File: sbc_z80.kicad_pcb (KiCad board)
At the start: 4 copper layers, 102.6 x 50.8 mm, 95 parts, among them J1 RC80 Bus, J2 CTC Header, J3 AVR-JTAG-10, J4 IDE, J5 PIO Header, J6 Port A, J7 Port B, J8 USB_B_Micro, Q1 IRLML6402, SW1 Reset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

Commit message: more routing
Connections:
- J1 pad 21: /CLK -> /CLK_CPU
- U3 pad 1: /CLK -> /CLK_CPU
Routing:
- net /D1: track 1.23 -> 186.7 mm, vias 1 -> 15
- net /D5: track 0.00 -> 179.5 mm, vias 0 -> 12
- net /D4: track 1.40 -> 170.8 mm, vias 0 -> 12
- net /D6: track 2.35 -> 168.4 mm, vias 1 -> 11
- net /IEI: track 0.00 -> 132.6 mm, vias 0 -> 6
- net /D7: track 0.00 -> 123.6 mm, vias 0 -> 6
- net /D3: track 0.00 -> 121.5 mm, vias 0 -> 12
- net /~M1: track 0.00 -> 114.5 mm, vias 0 -> 7
- net /D0: track 19.2 -> 121.3 mm, vias 0 -> 10
- net /~RESET: track 0.00 -> 101.2 mm, vias 0 -> 5
- net /D2: track 9.98 -> 110.8 mm, vias 2 -> 9
- net /CLK_CPU: track 0.00 -> 91.1 mm, vias 0 -> 6
- net /~IORQ: track 0.00 -> 75.4 mm, vias 0 -> 3
- net /~INT: track 0.00 -> 60.1 mm, vias 0 -> 3
- net /~WR: track 0.00 -> 58.1 mm, vias 0 -> 3
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
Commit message: cleanup
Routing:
- net /D7: track 123.6 -> 145.9 mm, vias 6 -> 7
- net /IEI: track 132.6 -> 134.1 mm
- net /D6: track 168.4 -> 167.6 mm
- net /PA4: track 27.4 -> 26.9 mm
- net /D3: track 121.5 -> 121.7 mm, vias 12 -> 11
- net /D1: vias 15 -> 14

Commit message: checkpoint
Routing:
- net /~IORQ: track 75.4 -> 0.00 mm, vias 3 -> 0
- net /~RTSB: track 0.00 -> 18.4 mm, vias 0 -> 3
- net /D2: track 110.4 -> 125.5 mm
- net /TXB: track 13.2 -> 27.8 mm, vias 0 -> 1
- net /~M1: track 114.5 -> 106.7 mm, vias 7 -> 6
- net /D7: track 145.9 -> 141.0 mm
- net /PA1: track 18.7 -> 20.5 mm
- net Net-(J7-Pad6): track 4.26 -> 5.92 mm, vias 0 -> 1
- net Net-(J7-Pad5): track 2.94 -> 4.38 mm, vias 0 -> 1
- net /PB2: track 9.20 -> 10.1 mm, vias 0 -> 1
- net /PB3: track 9.92 -> 10.8 mm, vias 0 -> 1
- net /TDI: track 4.12 -> 3.32 mm
- net /~ASTB: track 19.3 -> 18.5 mm
- net /D4: track 170.8 -> 171.6 mm
- net /A0: track 167.6 -> 166.9 mm
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- added copper zone on In2.Cu, net (none)
- removed copper zone on In2.Cu, net VCC

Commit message: routed...
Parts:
- C1, C10, C15, C16, C2, C5, C6, C8, C9, R10, R12, R13, R14, R15: moved to F.Cu
- moved R11 12.7 mm to (154.3, 105.2), turned to 0 degrees
- moved C16 5.97 mm to (164.5, 94.9), turned to 0 degrees
- moved C8 4.99 mm to (190.4, 91.6)
- moved C1 4.91 mm to (127.0, 115.7), turned to 270 degrees
- moved C5 4.84 mm to (127.0, 101.7), turned to 90 degrees
- moved C15 4.36 mm to (190.0, 107.2)
- moved C2 4.35 mm to (116.5, 107.3)
- moved C6 3.72 mm to (133.9, 92.3)
- moved C10 3.35 mm to (176.7, 99.7)
- moved C9 1.39 mm to (150.7, 98.8)
- moved Q1 1.02 mm to (116.3, 106.6)
- moved R35 0.64 mm to (196.6, 113.4)
- moved R9 0.64 mm to (109.1, 121.0)
- moved R6 0.63 mm to (109.1, 116.0)
- moved R7 0.63 mm to (109.1, 110.9)
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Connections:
- C13 pad 1: +5V -> VCC
- C14 pad 1: +5V -> VCC
- J1 pad 37: (no net) -> /USR1
- J1 pad 38: (no net) -> /USR2
- J1 pad 39: (no net) -> /USR3
- J1 pad 41: (no net) -> Net-(J1-Pad41)
- J1 pad 42: (no net) -> Net-(J1-Pad42)
- J1 pad 43: (no net) -> Net-(J1-Pad43)
- J1 pad 44: (no net) -> Net-(J1-Pad44)
- J1 pad 45: (no net) -> Net-(J1-Pad45)
- J1 pad 46: (no net) -> Net-(J1-Pad46)
- J1 pad 47: (no net) -> Net-(J1-Pad47)
- J1 pad 48: (no net) -> Net-(J1-Pad48)
- J1 pad 49: (no net) -> /A23
- J1 pad 50: (no net) -> /A22
- J1 pad 51: (no net) -> /A21
- J1 pad 52: (no net) -> /A20
- J1 pad 53: (no net) -> /A19
- J1 pad 61: (no net) -> /CLK2
- J1 pad 67: (no net) -> /D8
- J1 pad 68: (no net) -> /D9
- J1 pad 69: (no net) -> /D10
- J1 pad 70: (no net) -> /D11
- J1 pad 71: (no net) -> /D12
- J1 pad 72: (no net) -> /D13
- J1 pad 73: (no net) -> /D14
- J1 pad 74: (no net) -> /D15
- J1 pad 77: (no net) -> /USR5
- J1 pad 78: (no net) -> /USR6
- J1 pad 79: (no net) -> /USR7
- J2 pad 9: (no net) -> /CLKX
- J3 pad 7: (no net) -> Net-(J3-Pad7)
- J3 pad 8: (no net) -> Net-(J3-Pad8)
- J4 pad 10: (no net) -> Net-(J4-Pad10)
- J4 pad 12: (no net) -> Net-(J4-Pad12)
- J4 pad 14: (no net) -> Net-(J4-Pad14)
- J4 pad 16: (no net) -> Net-(J4-Pad16)
- J4 pad 18: (no net) -> Net-(J4-Pad18)
- J4 pad 21: (no net) -> Net-(J4-Pad21)
- J4 pad 27: (no net) -> Net-(J4-Pad27)
- J4 pad 28: (no net) -> Net-(J4-Pad28)
- J4 pad 31: (no net) -> Net-(J4-Pad31)
- J4 pad 32: (no net) -> Net-(J4-Pad32)
- J4 pad 4: (no net) -> Net-(J4-Pad4)
- J4 pad 6: (no net) -> Net-(J4-Pad6)
- J4 pad 8: (no net) -> Net-(J4-Pad8)
- J6 pad 3: (no net) -> Net-(J6-Pad3)
- J7 pad 3: (no net) -> Net-(J7-Pad3)
- J8 pad 2: (no net) -> Net-(J8-Pad2)
- J8 pad 3: (no net) -> Net-(J8-Pad3)
- J8 pad 4: (no net) -> Net-(J8-Pad4)
- U10 pad 2: (no net) -> Net-(U10-Pad2)
- U10 pad 28: (no net) -> Net-(U10-Pad28)
- U10 pad 39: (no net) -> Net-(U10-Pad39)
- U12 pad 4: (no net) -> Net-(U12-Pad4)
- U12 pad 5: +5V -> VCC
- U3 pad 11: (no net) -> Net-(U3-Pad11)
- U3 pad 17: (no net) -> Net-(U3-Pad17)
- U3 pad 33: (no net) -> Net-(U3-Pad33)
- U3 pad 39: (no net) -> Net-(U3-Pad39)
- U4 pad 11: (no net) -> Net-(U4-Pad11)
- U4 pad 15: (no net) -> Net-(U4-Pad15)
- U4 pad 17: (no net) -> Net-(U4-Pad17)
- U4 pad 20: (no net) -> Net-(U4-Pad20)
- U4 pad 24: (no net) -> Net-(U4-Pad24)
- U4 pad 26: (no net) -> Net-(U4-Pad26)
- U4 pad 28: (no net) -> Net-(U4-Pad28)
- U4 pad 30: (no net) -> Net-(U4-Pad30)
- U4 pad 31: /~SIO -> /~CTC
- U4 pad 34: (no net) -> Net-(U4-Pad34)
- U4 pad 38: (no net) -> Net-(U4-Pad38)
- U4 pad 39: (no net) -> Net-(U4-Pad39)
- U4 pad 42: (no net) -> Net-(U4-Pad42)
- U4 pad 44: (no net) -> Net-(U4-Pad44)
- U4 pad 5: (no net) -> Net-(U4-Pad5)
- U4 pad 6: (no net) -> Net-(U4-Pad6)
- U4 pad 7: (no net) -> Net-(U4-Pad7)
- U5 pad 20: (no net) -> Net-(U5-Pad20)
- U5 pad 21: (no net) -> Net-(U5-Pad21)
- U5 pad 22: (no net) -> /~PIO_RST
- U5 pad 31: (no net) -> /~CTC
- U9 pad 1: (no net) -> Net-(U9-Pad1)
- U9 pad 10: (no net) -> Net-(U9-Pad10)
- U9 pad 15: (no net) -> Net-(U9-Pad15)
- U9 pad 16: (no net) -> Net-(U9-Pad16)
- U9 pad 17: (no net) -> Net-(U9-Pad17)
- U9 pad 27: (no net) -> /DO
- U9 pad 28: (no net) -> Net-(U9-Pad28)
- U9 pad 38: (no net) -> Net-(U9-Pad38)
- U9 pad 39: (no net) -> Net-(U9-Pad39)
- U9 pad 40: (no net) -> Net-(U9-Pad40)
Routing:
- net /~IORQ: track 0.00 -> 170.4 mm, vias 0 -> 10
- net /~RD: track 21.8 -> 192.0 mm, vias 3 -> 12
- net /CLK_U: track 6.93 -> 143.0 mm, vias 0 -> 5
- net /IEO: track 0.00 -> 136.1 mm, vias 0 -> 5
- net /D2: track 125.5 -> 226.4 mm, vias 9 -> 13
- net /~RESET: track 101.2 -> 190.3 mm, vias 5 -> 13
- net VCC: track 0.00 -> 86.8 mm, vias 0 -> 35
- net /D0: track 121.1 -> 206.6 mm, vias 10 -> 14
- net /~SIO: track 0.00 -> 79.1 mm, vias 0 -> 3
- net /D3: track 122.3 -> 199.8 mm, vias 10 -> 12
- net /D7: track 141.0 -> 208.4 mm, vias 7 -> 10
- net GND: track 0.00 -> 66.7 mm, vias 0 -> 36
- net /~INT: track 60.5 -> 125.8 mm, vias 3 -> 8
- net /D4: track 171.6 -> 235.6 mm, vias 12 -> 13
- net /~RAM: track 0.00 -> 63.8 mm, vias 0 -> 2
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- added copper zone on In2.Cu, net VCC
- removed copper zone on In2.Cu, net (none)

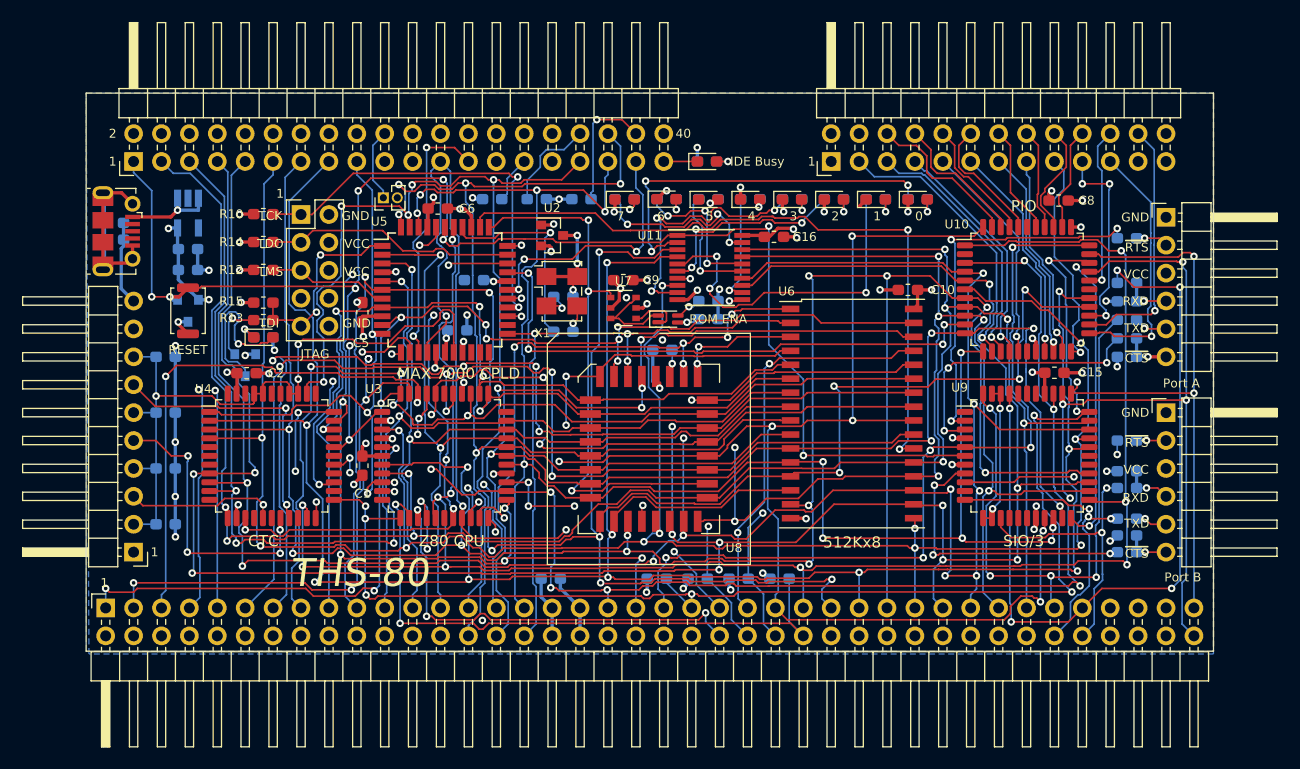
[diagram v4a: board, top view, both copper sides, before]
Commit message: passed drc
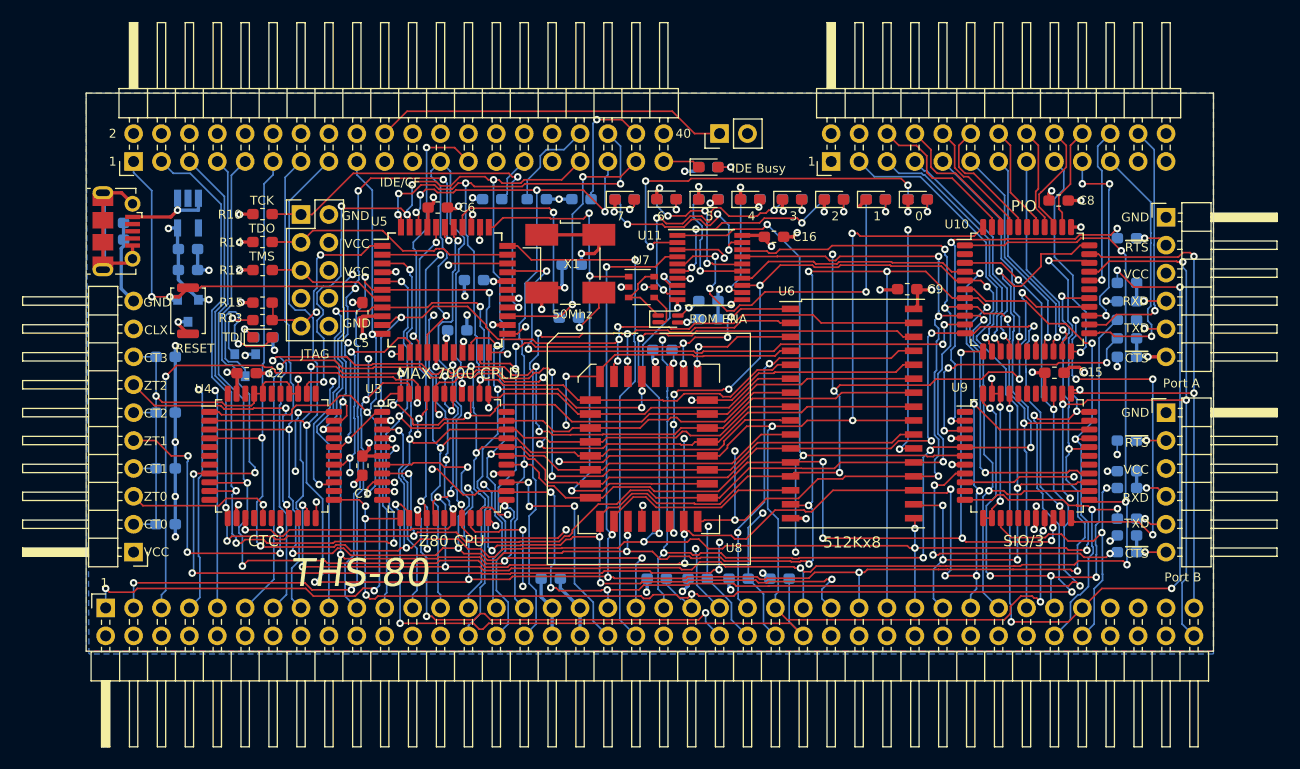
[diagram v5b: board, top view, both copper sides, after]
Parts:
- removed C10: 100nF, Capacitor_SMD:C_0603_1608Metric_Pad1.05x0.95mm_HandSolder
- removed G***: LOGO, Logos:asian_tiger
- removed U2: AP7381-33SA, Package_TO_SOT_SMD:SOT-23
- C13: value 10uF -> 1uF
- C14: value 1uF -> 100nF
- JP1: footprint Connector_PinHeader_1.27mm:PinHeader_1x02_P1.27mm_Vertical -> Connector_PinHeader_2.54mm:PinHeader_1x02_P2.54mm_Vertical
- X1: value CTX-636 50mhz -> CFPS-72 50mhz; footprint Oscillator:Oscillator_SMD_TXC_7C-4Pin_5.0x3.2mm_HandSoldering -> Oscillator:Oscillator_SMD_SeikoEpson_SG8002CA-4Pin_7.0x5.0mm_HandSoldering
- moved JP1 31.2 mm to (159.5, 85.5)
- moved C9 25.9 mm to (176.6, 99.6)
- moved C7 3.02 mm to (146.1, 97.4)
- moved X1 2.62 mm to (145.9, 97.3)
- moved U7 2.52 mm to (152.4, 99.4)
- moved R3 1.37 mm to (145.8, 102.2)
- moved D2 0.52 mm to (158.5, 88.5)
- moved R16 0.52 mm to (158.5, 88.5)
- moved C6 0.09 mm to (133.9, 92.2)
- moved D1 0.08 mm to (117.9, 104.0)
- moved R10 0.08 mm to (117.9, 92.8)
- moved R13 0.08 mm to (117.9, 102.4)
- moved R14 0.08 mm to (117.9, 95.3)
- moved R15 0.08 mm to (117.9, 100.9)
- moved R12 0.07 mm to (117.9, 97.9)
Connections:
- net /~CTC renamed /CTC_~CE~
- net /~PIO renamed /PIO_~CE~
- net /~RAM renamed /RAM_~CE~
- net /~ROM renamed /ROM_~CE~
- C7 pad 1: /3V3 -> VCC
- J1 pad 37: /USR1 -> (no net)
- J1 pad 38: /USR2 -> (no net)
- J1 pad 39: /USR3 -> (no net)
- J1 pad 41: Net-(J1-Pad41) -> (no net)
- J1 pad 42: Net-(J1-Pad42) -> (no net)
- J1 pad 43: Net-(J1-Pad43) -> (no net)
- J1 pad 44: Net-(J1-Pad44) -> (no net)
- J1 pad 45: Net-(J1-Pad45) -> (no net)
- J1 pad 46: Net-(J1-Pad46) -> (no net)
- J1 pad 47: Net-(J1-Pad47) -> (no net)
- J1 pad 48: Net-(J1-Pad48) -> (no net)
- J1 pad 49: /A23 -> (no net)
- J1 pad 50: /A22 -> (no net)
- J1 pad 51: /A21 -> (no net)
- J1 pad 52: /A20 -> (no net)
- J1 pad 53: /A19 -> (no net)
- J1 pad 61: /CLK2 -> (no net)
- J1 pad 67: /D8 -> (no net)
- J1 pad 68: /D9 -> (no net)
- J1 pad 69: /D10 -> (no net)
- J1 pad 70: /D11 -> (no net)
- J1 pad 71: /D12 -> (no net)
- J1 pad 72: /D13 -> (no net)
- J1 pad 73: /D14 -> (no net)
- J1 pad 74: /D15 -> (no net)
- J1 pad 77: /USR5 -> (no net)
- J1 pad 78: /USR6 -> (no net)
- J1 pad 79: /USR7 -> (no net)
- J2 pad 9: /CLKX -> (no net)
- J3 pad 7: Net-(J3-Pad7) -> (no net)
- J3 pad 8: Net-(J3-Pad8) -> (no net)
- J4 pad 10: Net-(J4-Pad10) -> (no net)
- J4 pad 12: Net-(J4-Pad12) -> (no net)
- J4 pad 14: Net-(J4-Pad14) -> (no net)
- J4 pad 16: Net-(J4-Pad16) -> (no net)
- J4 pad 18: Net-(J4-Pad18) -> (no net)
- J4 pad 21: Net-(J4-Pad21) -> (no net)
- J4 pad 27: Net-(J4-Pad27) -> (no net)
- J4 pad 28: Net-(J4-Pad28) -> (no net)
- J4 pad 31: Net-(J4-Pad31) -> (no net)
- J4 pad 32: Net-(J4-Pad32) -> (no net)
- J4 pad 37: /~CF -> /IDE_~CE~
- J4 pad 4: Net-(J4-Pad4) -> (no net)
- J4 pad 6: Net-(J4-Pad6) -> (no net)
- J4 pad 8: Net-(J4-Pad8) -> (no net)
- J6 pad 3: Net-(J6-Pad3) -> (no net)
- J7 pad 3: Net-(J7-Pad3) -> (no net)
- J8 pad 2: Net-(J8-Pad2) -> (no net)
- J8 pad 3: Net-(J8-Pad3) -> (no net)
- J8 pad 4: Net-(J8-Pad4) -> (no net)
- U10 pad 2: Net-(U10-Pad2) -> (no net)
- U10 pad 28: Net-(U10-Pad28) -> (no net)
- U10 pad 39: Net-(U10-Pad39) -> (no net)
- U12 pad 4: Net-(U12-Pad4) -> (no net)
- U3 pad 11: Net-(U3-Pad11) -> (no net)
- U3 pad 17: Net-(U3-Pad17) -> (no net)
- U3 pad 33: Net-(U3-Pad33) -> (no net)
- U3 pad 39: Net-(U3-Pad39) -> (no net)
- U4 pad 11: Net-(U4-Pad11) -> (no net)
- U4 pad 15: Net-(U4-Pad15) -> (no net)
- U4 pad 17: Net-(U4-Pad17) -> (no net)
- U4 pad 20: Net-(U4-Pad20) -> (no net)
- U4 pad 24: Net-(U4-Pad24) -> (no net)
- U4 pad 26: Net-(U4-Pad26) -> (no net)
- U4 pad 28: Net-(U4-Pad28) -> (no net)
- U4 pad 30: Net-(U4-Pad30) -> (no net)
- U4 pad 34: Net-(U4-Pad34) -> (no net)
- U4 pad 38: Net-(U4-Pad38) -> (no net)
- U4 pad 39: Net-(U4-Pad39) -> (no net)
- U4 pad 42: Net-(U4-Pad42) -> (no net)
- U4 pad 44: Net-(U4-Pad44) -> (no net)
- U4 pad 5: Net-(U4-Pad5) -> (no net)
- U4 pad 6: Net-(U4-Pad6) -> (no net)
- U4 pad 7: Net-(U4-Pad7) -> (no net)
- U5 pad 18: /CLK_U -> /CLK_UART
- U5 pad 20: Net-(U5-Pad20) -> /A18
- U5 pad 21: Net-(U5-Pad21) -> /A17
- U5 pad 22: /~PIO_RST -> /A16
- U5 pad 23: /A16 -> /D_LED
- U5 pad 25: /D_LED -> /IDE_~CE~
- U5 pad 27: /~PAGE -> /SIO_~CE~
- U5 pad 28: /~CF -> (no net)
- U5 pad 33: /~SIO -> /~PAGE
- U9 pad 1: Net-(U9-Pad1) -> (no net)
- U9 pad 10: Net-(U9-Pad10) -> (no net)
- U9 pad 12: /CLK_U -> /CLK_UART
- U9 pad 13: /CLK_U -> /CLK_UART
- U9 pad 15: Net-(U9-Pad15) -> (no net)
- U9 pad 16: Net-(U9-Pad16) -> (no net)
- U9 pad 17: Net-(U9-Pad17) -> (no net)
- U9 pad 22: /~SIO -> /SIO_~CE~
- U9 pad 27: /DO -> (no net)
- U9 pad 28: Net-(U9-Pad28) -> (no net)
- U9 pad 38: Net-(U9-Pad38) -> (no net)
- U9 pad 39: Net-(U9-Pad39) -> (no net)
- U9 pad 40: Net-(U9-Pad40) -> (no net)
- U9 pad 42: /CLK_U -> /CLK_UART
- U9 pad 43: /CLK_U -> /CLK_UART
- X1 pad 1: /3V3 -> VCC
- X1 pad 4: /3V3 -> VCC
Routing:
- net /CLK_U: track 143.0 -> 40.8 mm, vias 5 -> 2
- net /SIO_~CE~: track 0.00 -> 87.8 mm, vias 0 -> 5
- net /~SIO: track 79.1 -> 0.00 mm, vias 3 -> 0
- net /CLK_UART: track 0.00 -> 65.5 mm, vias 0 -> 4
- net Net-(J4-Pad20): track 6.68 -> 32.2 mm
- net /IDE_~CE~: track 0.00 -> 23.8 mm, vias 0 -> 2
- net /~CF: track 23.6 -> 0.00 mm, vias 3 -> 0
- net /3V3: track 9.29 -> 0.00 mm, vias 3 -> 0
- net /A18: track 71.3 -> 79.6 mm, vias 4 -> 5
- net /D0: track 206.6 -> 199.8 mm, vias 14 -> 15
- net /~PAGE: track 42.8 -> 47.6 mm, vias 2 -> 1
- net /A16: track 59.0 -> 63.0 mm, vias 3 -> 4
- net /A17: track 59.5 -> 63.5 mm, vias 5 -> 6
- net /~BUSACK: track 32.3 -> 28.7 mm
- net /CLK_CPU: track 138.1 -> 141.3 mm
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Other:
- board text added: "50Mhz"
- board text added: "CLX"
- board text added: "CT0"
- board text added: "CT1"
- board text added: "CT2"
- board text added: "CT3"
- board text added: "IDE/CF"
- board text added: "ZT0"
- board text added: "ZT1"
- board text added: "ZT2"
